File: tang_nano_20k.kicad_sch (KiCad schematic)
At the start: 5 parts, among them J3 Conn_Coaxial, U2 Tang_Nano_20K, U5 Adafruit_PCM510x

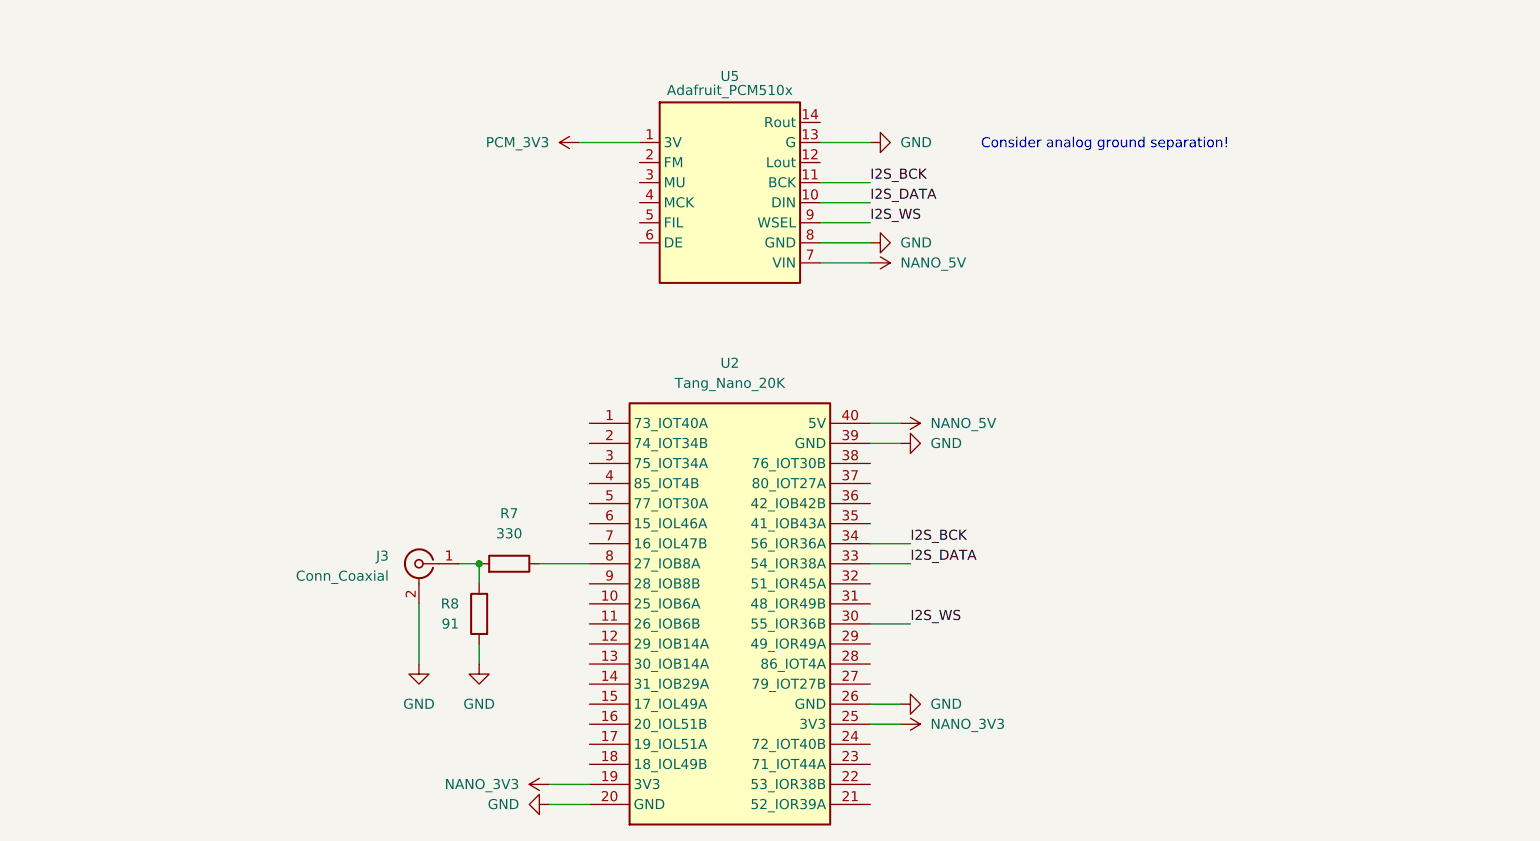
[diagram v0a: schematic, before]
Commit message: Add extra SPDIF out plus pin header taps for SPDIF and I2S
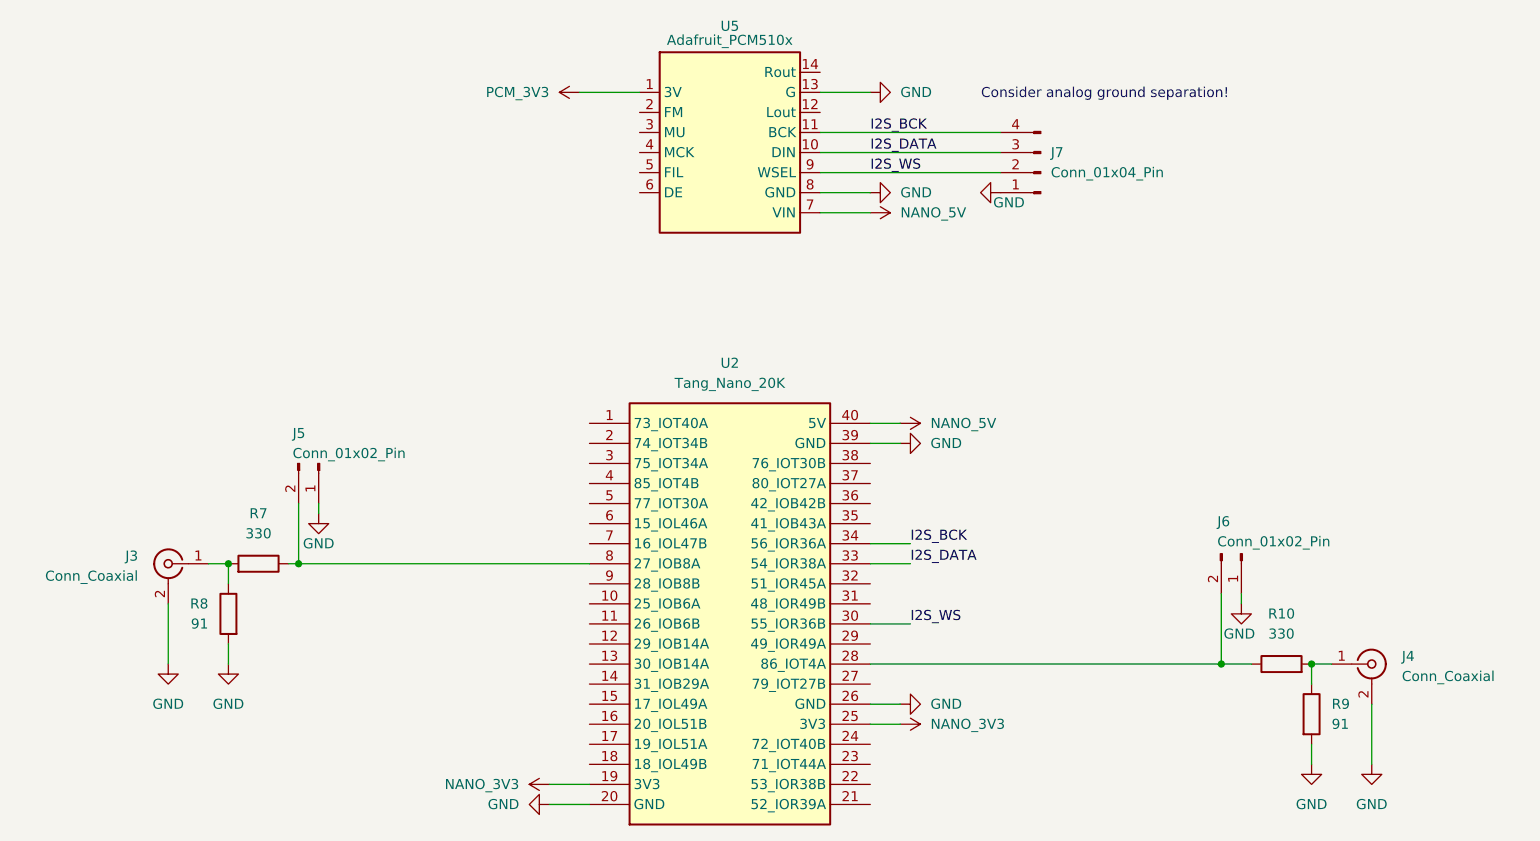
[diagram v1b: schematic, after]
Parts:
- added J4: Conn_Coaxial, symbol Connector:Conn_Coaxial
- added J5, J6: Conn_01x02_Pin, LED_THT:LED_D5.0mm_IRGrey, symbol Connector:Conn_01x02_Pin
- added J7: Conn_01x04_Pin, symbol Connector:Conn_01x04_Pin
- added R10: 330, symbol Device:R
- added R9: 91, symbol Device:R
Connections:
- net GND: now also J4.2 (Ext), J5.1 (Pin_1), J6.1 (Pin_1), J7.1 (Pin_1), R9.2
- net I2S_BCK: now also J7.4 (Pin_4)
- net I2S_DATA: now also J7.3 (Pin_3)
- net I2S_WS: now also J7.2 (Pin_2)
- net at U2.28 (86_IOT4A): now also J6.2 (Pin_2), R10.1
- net at R7.1, U2.8 (27_IOB8A): now also J5.2 (Pin_2)
- new net: J4.1 (In), R10.2, R9.1
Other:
- moved on the sheet: J3, R7, R8, U5

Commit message: Switched to global net labels, reorganised header connectors.
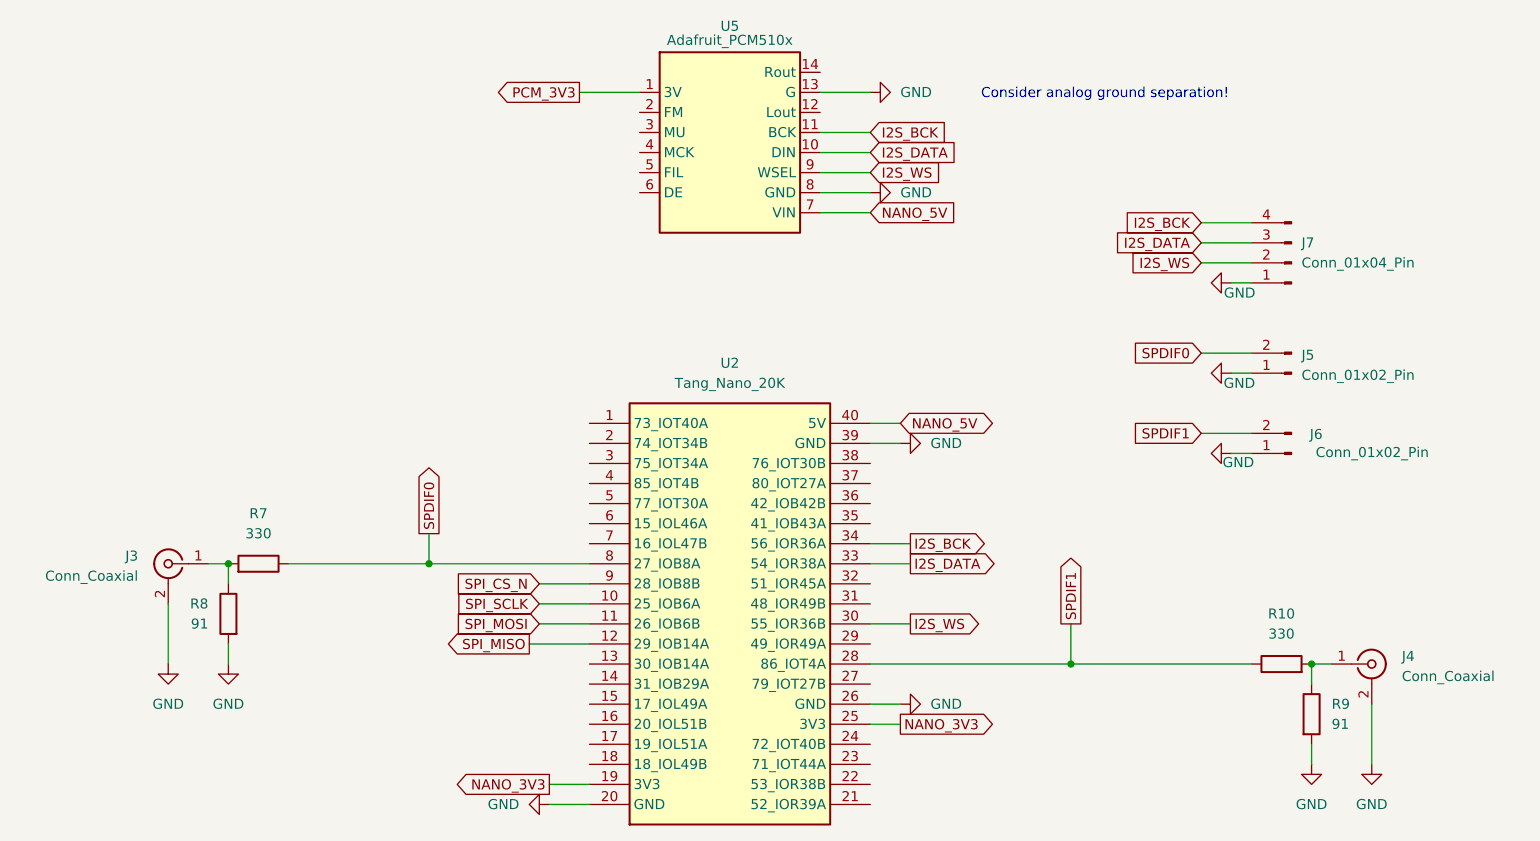
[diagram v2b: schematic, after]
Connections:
- net SPDIF1: now reaches J6.2 (Pin_2), R10.1, U2.28 (86_IOT4A)
- net SPI_SCLK: now reaches U2.10 (25_IOB6A)
- net SPI_MOSI: now reaches U2.11 (26_IOB6B)
- net SPI_MISO: now reaches U2.12 (29_IOB14A)
- net SPDIF0: now reaches J5.2 (Pin_2), R7.1, U2.8 (27_IOB8A)
- net SPI_CS_N: now reaches U2.9 (28_IOB8B)
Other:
- moved on the sheet: J5, J6, J7
